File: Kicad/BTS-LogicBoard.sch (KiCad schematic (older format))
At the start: 54 parts, among them J1 Conn_02x03_Odd_Even, J2 Conn_01x03, J3 Conn_01x02, J4 Conn_02x03_Odd_Even, J5 Conn_01x06, Q1 BC817, U1 NCS2252SN2T1G, U2 NE555DR/TS555, U3 74HC1GU04, U4 TLP291, U5 74HC1GU04, U6 NCS2252SN2T1G, U8 LM1117-5.0

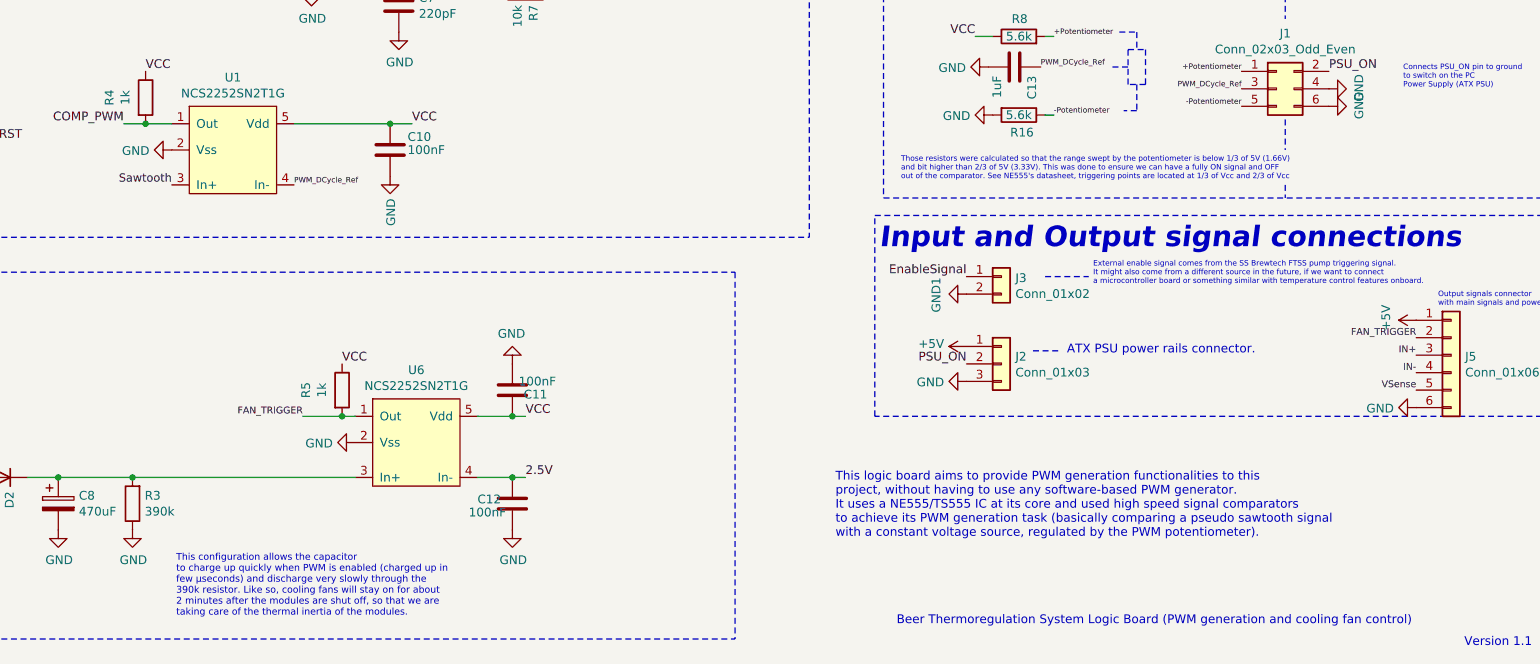
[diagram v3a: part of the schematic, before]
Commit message: Added hysteresis resistor to comparators and reexported gerbers
Signed-off-by: bebenlebricolo <benoittarrade@hotmail.fr>
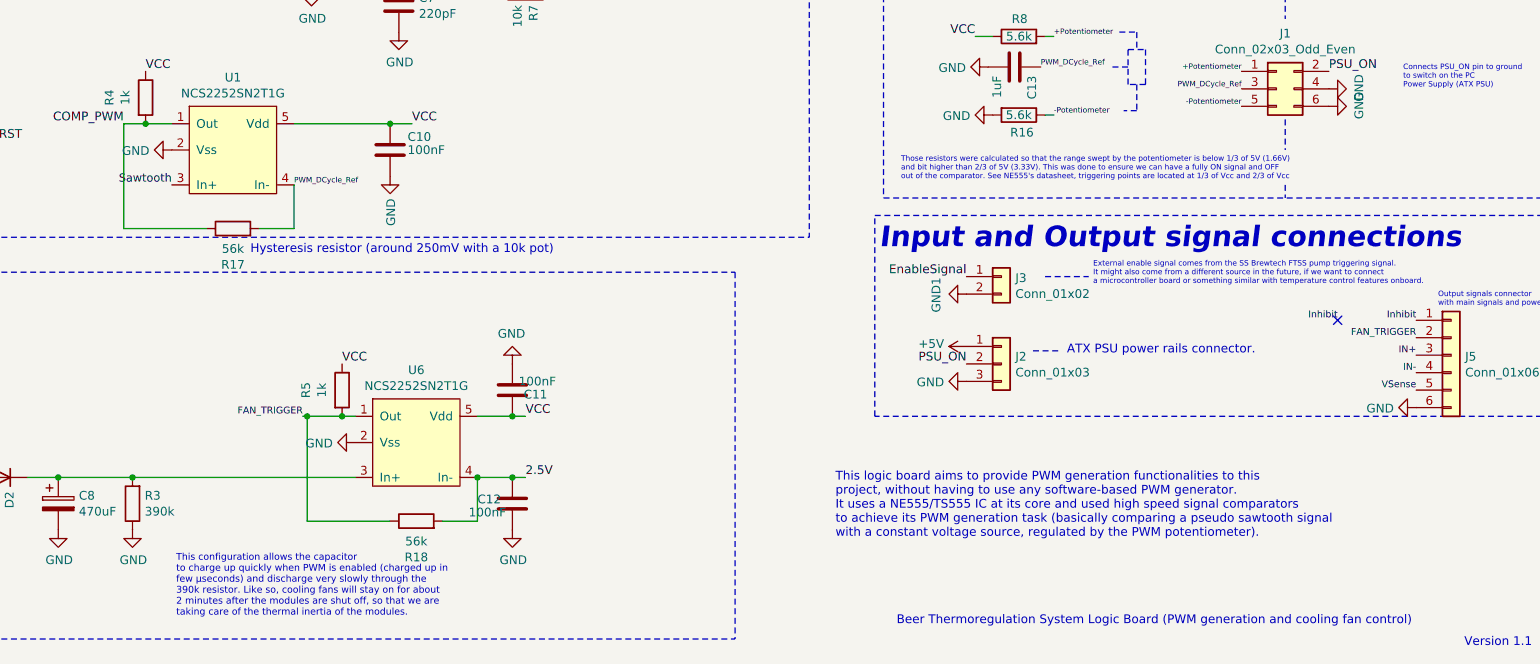
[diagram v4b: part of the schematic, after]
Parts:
- added R17, R18: 56k, Resistor_SMD:R_1206_3216Metric_Pad1.30x1.75mm_HandSolder, symbol Device:R
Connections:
- net +5V: no longer J5.1 (Pin_1)
- net 2.5V: now also R18.2
- net COMP_PWM: now also R17.1
- net FAN_TRIGGER: now also R18.1
- net PWM_DCycle_Ref: now also R17.2
- new net Inhibit: J5.1 (Pin_1)
- no-connect marks 0 -> 1
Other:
- note added: "Hysteresis resistor (around 250mV with a 10k pot)"
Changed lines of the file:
@@
 $EndDescr
-$Comp
-L BTS-LogicBoard:NCS2252SN2T1G U1
-U 1 1 613B3E2B
-P 3600 5025
-F 0 "U1" H 3600 5690 50  0000 C CNN
-F 1 "NCS2252SN2T1G" H 3600 5599 50  0000 C CNN
-F 2 "Package_TO_SOT_SMD:SOT-23-5" H 3600 5025 50  0001 C CNN
-F 3 "" H 3600 5025 50  0001 C CNN
-	1    3600 5025
-	1    0    0    -1
-$EndComp
 $Comp
 L power:GND #PWR0101
@@
 	4225 6300 4300 6300
 Wire Wire Line
-	4225 6300 4000 6300
+	4225 6300 4025 6300
 Connection ~ 4225 6300
 Wire Wire Line
@@
 $EndComp
 $Comp
-L power:+5V #PWR025
-U 1 1 617CD945
-P 10375 5750
-F 0 "#PWR025" H 10375 5600 50  0001 C CNN
-F 1 "+5V" H 10390 5923 50  0000 C CNN
-F 2 "" H 10375 5750 50  0001 C CNN
-F 3 "" H 10375 5750 50  0001 C CNN
-	1    10375 5750
-	0    -1   -1   0
-$EndComp
+L BTS-LogicBoard:NCS2252SN2T1G U1
+U 1 1 613B3E2B
+P 3600 5025
+F 0 "U1" H 3600 5690 50  0000 C CNN
+F 1 "NCS2252SN2T1G" H 3600 5599 50  0000 C CNN
+F 2 "Package_TO_SOT_SMD:SOT-23-5" H 3600 5025 50  0001 C CNN
+F 3 "" H 3600 5025 50  0001 C CNN
+	1    3600 5025
+	1    0    0    -1
+$EndComp
+$Comp
+L Device:R R17
+U 1 1 616943E6
+P 3600 5225
+F 0 "R17" V 3393 5225 50  0000 C CNN
+F 1 "56k" V 3484 5225 50  0000 C CNN
+F 2 "Resistor_SMD:R_1206_3216Metric_Pad1.30x1.75mm_HandSolder" V 3530 5225 50  0001 C CNN
+F 3 "~" H 3600 5225 50  0001 C CNN
+	1    3600 5225
+	0    -1   -1   0
+$EndComp
+Wire Wire Line
+	3450 5225 2975 5225
+Wire Wire Line
+	2975 5225 2975 4625
+Wire Wire Line
+	3750 5225 3950 5225
+Wire Wire Line
+	3950 5225 3950 4975
+Text Notes 3700 5375 0    50   ~ 0
+Hysteresis resistor (around 250mV with a 10k pot)
+$Comp
+L Device:R R18
+U 1 1 6169D276
+P 4650 6900
+F 0 "R18" V 4443 6900 50  0000 C CNN
+F 1 "56k" V 4534 6900 50  0000 C CNN
+F 2 "Resistor_SMD:R_1206_3216Metric_Pad1.30x1.75mm_HandSolder" V 4580 6900 50  0001 C CNN
+F 3 "~" H 4650 6900 50  0001 C CNN
+	1    4650 6900
+	0    -1   -1   0
+$EndComp
+Wire Wire Line
+	5000 6650 5000 6900
+Wire Wire Line
+	5000 6900 4800 6900
+Connection ~ 5000 6650
+Wire Wire Line
+	4500 6900 4025 6900
+Wire Wire Line
+	4025 6900 4025 6300
+Connection ~ 4025 6300
+Wire Wire Line
+	4025 6300 4000 6300
+Text Label 10375 5750 2    39   ~ 0
+Inhibit
+Text Label 9925 5750 2    39   ~ 0
+Inhibit
+NoConn ~ 9925 5750
 $EndSCHEMATC

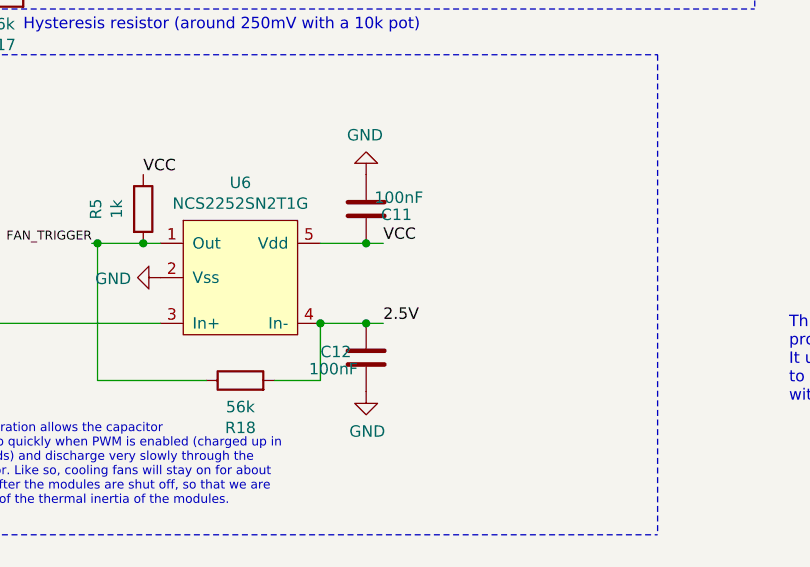
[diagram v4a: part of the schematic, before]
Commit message: Forgot to add another hysteresis resistor : done
Signed-off-by: bebenlebricolo <benoittarrade@hotmail.fr>
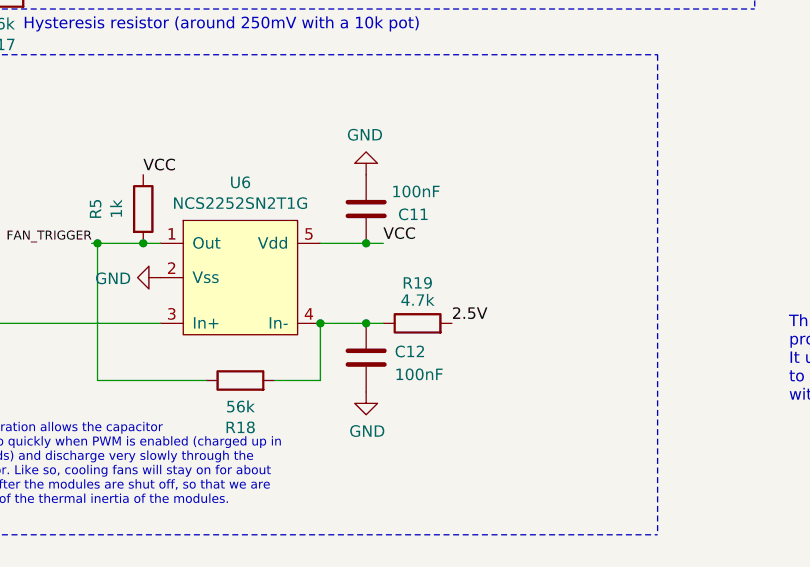
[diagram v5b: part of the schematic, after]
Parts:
- added R19: 4.7k, Resistor_SMD:R_1206_3216Metric_Pad1.30x1.75mm_HandSolder, symbol Device:R
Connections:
- net 2.5V: now also R19.2; no longer C12.1, R18.2, U6.4 (In-)
- new net: C12.1, R18.2, R19.1, U6.4 (In-)
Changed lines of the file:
@@
 Text Label 5275 6300 0    50   ~ 0
 VCC
-Text Label 5275 6650 0    50   ~ 0
+Text Label 5575 6650 0    50   ~ 0
 2.5V
 Text Notes 3275 7450 0    39   ~ 0
@@
 U 1 1 6180F799
 P 5200 6800
-F 0 "C12" H 5000 6825 50  0000 L CNN
-F 1 "100nF" H 4950 6750 50  0000 L CNN
+F 0 "C12" H 5325 6825 50  0000 L CNN
+F 1 "100nF" H 5325 6725 50  0000 L CNN
 F 2 "Capacitor_SMD:C_1206_3216Metric_Pad1.33x1.80mm_HandSolder" H 5238 6650 50  0001 C CNN
 F 3 "~" H 5200 6800 50  0001 C CNN
@@
 U 1 1 61812760
 P 5200 6150
-F 0 "C11" H 5000 6175 50  0000 L CNN
-F 1 "100nF" H 4950 6100 50  0000 L CNN
+F 0 "C11" H 4925 6175 50  0000 L CNN
+F 1 "100nF" H 4875 6075 50  0000 L CNN
 F 2 "Capacitor_SMD:C_1206_3216Metric_Pad1.33x1.80mm_HandSolder" H 5238 6000 50  0001 C CNN
 F 3 "~" H 5200 6150 50  0001 C CNN
@@
 Inhibit
 NoConn ~ 9925 5750
+$Comp
+L Device:R R19
+U 1 1 6169CBB7
+P 5425 6650
+F 0 "R19" V 5600 6650 50  0000 C CNN
+F 1 "4.7k" V 5525 6650 50  0000 C CNN
+F 2 "Resistor_SMD:R_1206_3216Metric_Pad1.30x1.75mm_HandSolder" V 5355 6650 50  0001 C CNN
+F 3 "~" H 5425 6650 50  0001 C CNN
+	1    5425 6650
+	0    -1   -1   0
+$EndComp
 $EndSCHEMATC

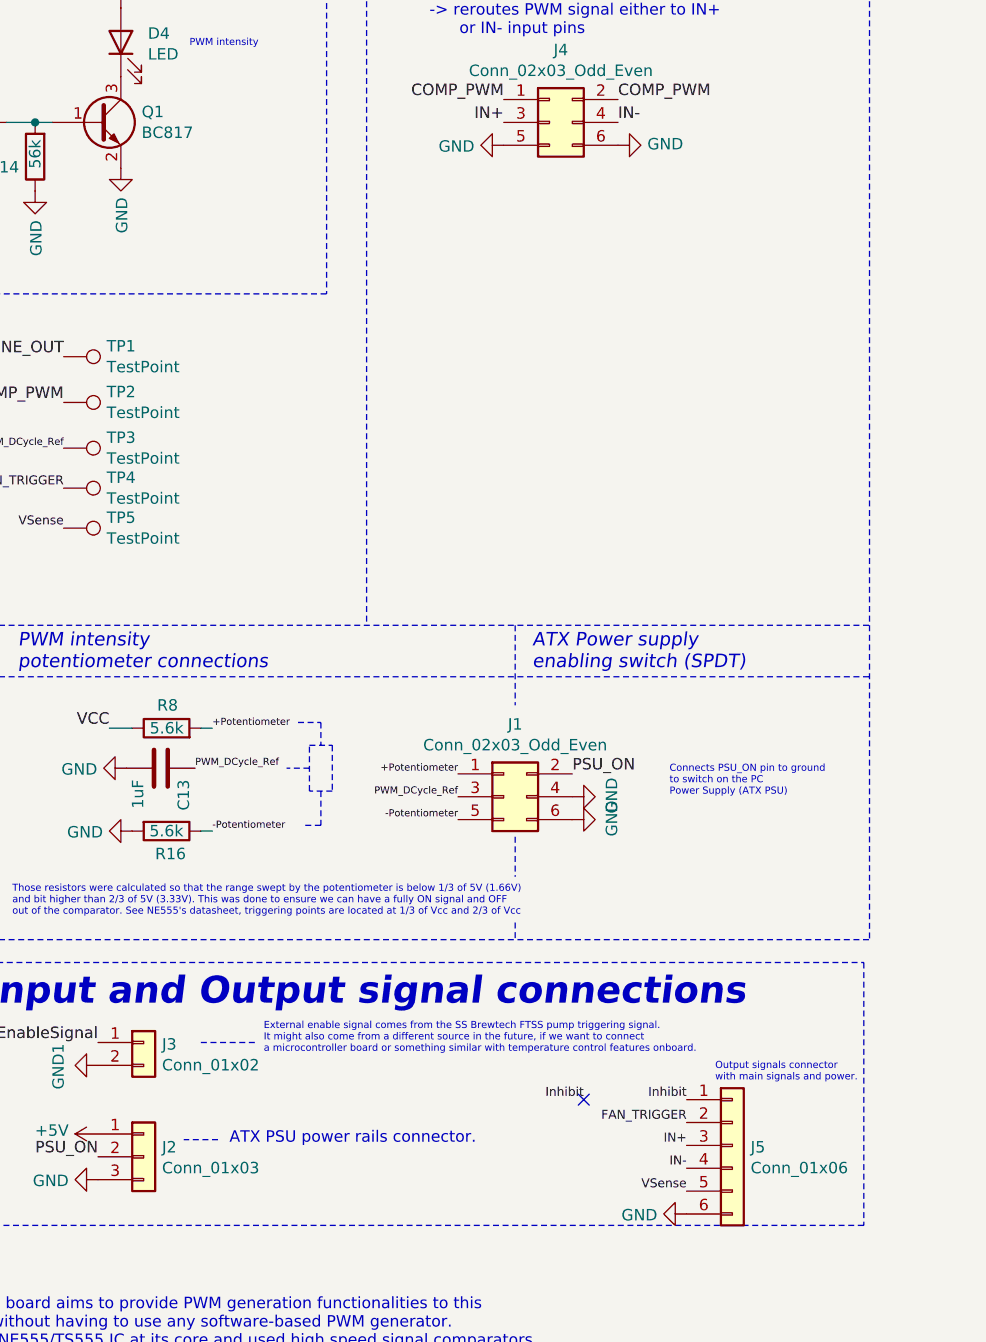
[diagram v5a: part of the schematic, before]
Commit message: Annotated schematic
Signed-off-by: bebenlebricolo <benoittarrade@hotmail.fr>
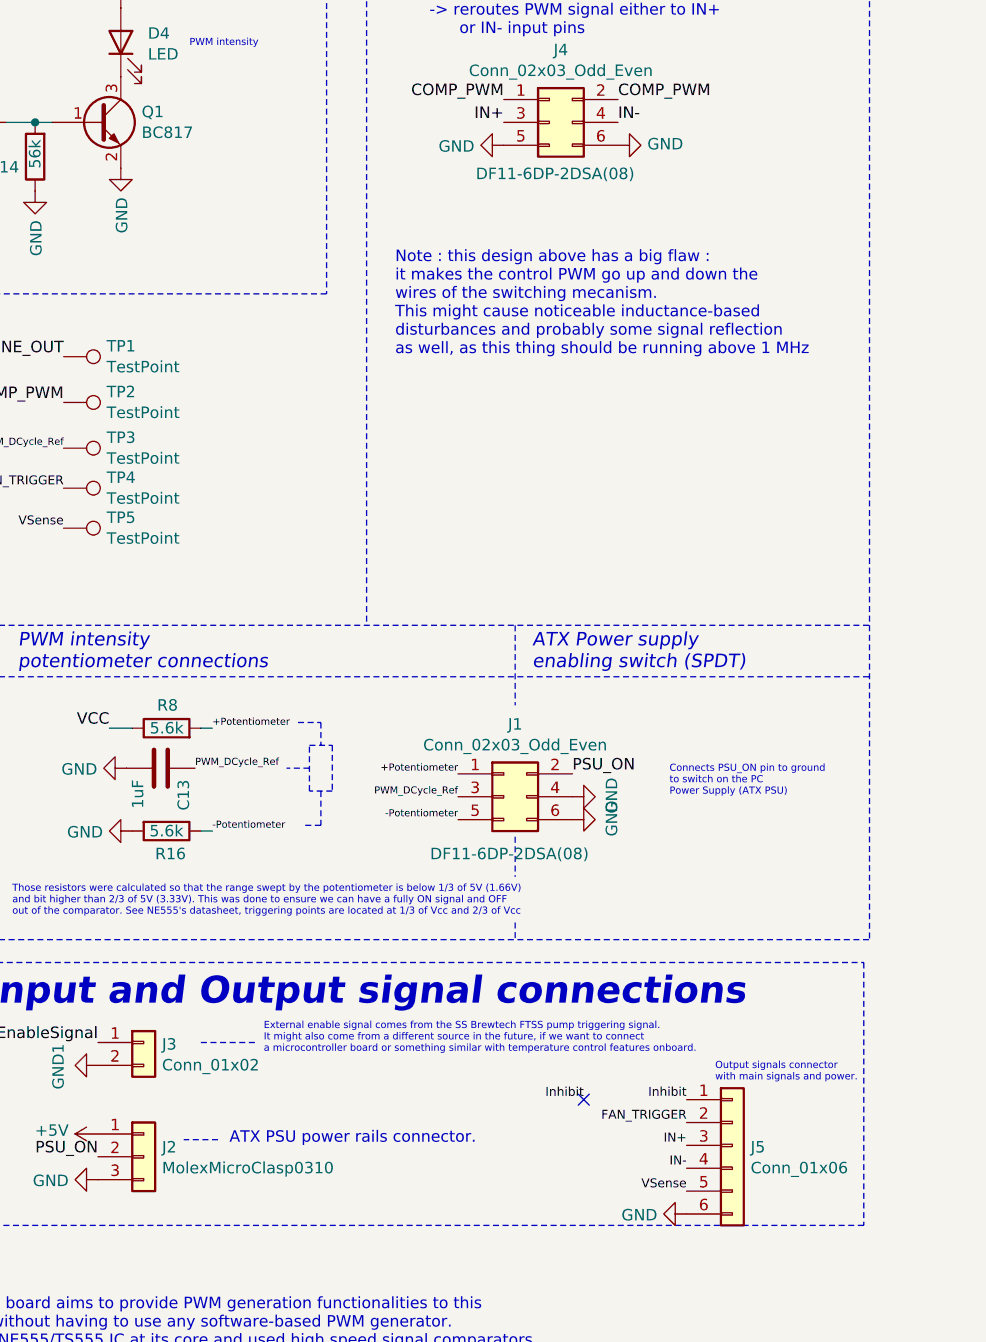
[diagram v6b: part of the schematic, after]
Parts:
- J1, J4: PartNumber (none) -> DF11-6DP-2DSA(08)
- J2: value Conn_01x03 -> MolexMicroClasp0310; PartNumber (none) -> 55935-0310; Series (none) -> Molex MicroClasp 3 pins, 3Amps
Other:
- note added: "Note : this design above has a big flaw : \nit makes the control PWM go up and down the\nwires of the switching mecanism.\nThis might cause noticeable inductance-based \ndisturbances and probably some signal reflection\nas well, as this thing should be running above 1 MHz"
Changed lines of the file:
@@
 P 8000 6000
 F 0 "J2" H 8080 6042 50  0000 L CNN
-F 1 "Conn_01x03" H 8080 5951 50  0000 L CNN
+F 1 "MolexMicroClasp0310" H 8080 5951 50  0000 L CNN
 F 2 "BTS-LogicBoard:559350310" H 8000 6000 50  0001 C CNN
 F 3 "~" H 8000 6000 50  0001 C CNN
+F 4 "55935-0310" H 8000 6000 50  0001 C CNN "PartNumber"
+F 5 "Molex MicroClasp 3 pins, 3Amps" H 8000 6000 50  0001 C CNN "Series"
 	1    8000 6000
 	1    0    0    -1
@@
 F 2 "Connector_Hirose:Hirose_DF11-6DP-2DSA_2x03_P2.00mm_Vertical" H 9775 1475 50  0001 C CNN
 F 3 "~" H 9775 1475 50  0001 C CNN
+F 4 "DF11-6DP-2DSA(08)" H 9800 1250 50  0000 C CNN "PartNumber"
 	1    9775 1475
 	1    0    0    -1
@@
 F 2 "Connector_Hirose:Hirose_DF11-6DP-2DSA_2x03_P2.00mm_Vertical" H 9575 4425 50  0001 C CNN
 F 3 "~" H 9575 4425 50  0001 C CNN
+F 4 "DF11-6DP-2DSA(08)" H 9600 4175 50  0000 C CNN "PartNumber"
 	1    9575 4425
 	1    0    0    -1
@@
 	0    -1   -1   0
 $EndComp
+Text Notes 9100 2500 0    50   ~ 0
+Note : this design above has a big flaw : \nit makes the control PWM go up and down the\nwires of the switching mecanism.\nThis might cause noticeable inductance-based \ndisturbances and probably some signal reflection\nas well, as this thing should be running above 1 MHz
 $EndSCHEMATC
